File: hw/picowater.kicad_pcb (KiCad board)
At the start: 2 copper layers, 80 x 58.8 mm, 7 parts, among them J1 Conn_01x04_MountingPin, J2 Conn_01x02_MountingPin, J3 Conn_01x06_Pin, U1 Pico

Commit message: v0.1
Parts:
- added J4: UART, Connector_PinHeader_2.54mm:PinHeader_1x03_P2.54mm_Vertical, F.Cu at (105.5, 114.2)
- moved J3 51.3 mm to (70.5, 118.5), turned to -90 degrees
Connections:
- J3 pad 1: GND -> unconnected-(J3-Pin_1-Pad1)
- J3 pad 2: unconnected-(J3-Pin_2-Pad2) -> Net-(J3-Pin_2)
- J3 pad 5: Net-(J3-Pin_5) -> unconnected-(J3-Pin_5-Pad5)
- J3 pad 6: unconnected-(J3-Pin_6-Pad6) -> GND
- U1 pad 14: Net-(J3-Pin_5) -> Net-(J3-Pin_4)
- U1 pad 15: Net-(J3-Pin_4) -> Net-(J3-Pin_3)
- U1 pad 16: Net-(J3-Pin_3) -> Net-(J3-Pin_2)
- U1 pad 21: unconnected-(U1-GPIO16-Pad21) -> Net-(J4-Pin_3)
- U1 pad 22: unconnected-(U1-GPIO17-Pad22) -> Net-(J4-Pin_2)
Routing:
- net Net-(J3-Pin_5): track 41.3 -> 0.00 mm
- net Net-(J3-Pin_3): track 51.4 -> 19.5 mm
- net Net-(J3-Pin_4): track 44.9 -> 23.1 mm
- net Net-(J3-Pin_2): track 0.00 -> 15.9 mm
- net +5V: track 59.0 -> 43.5 mm
- net Net-(J4-Pin_3): track 0.00 -> 7.72 mm
- net Net-(J4-Pin_2): track 0.00 -> 7.72 mm
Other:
- board text added: "+"
- board text added: "5v"
- board text added: "GND"
- board text added: "RX"
- board text added: "TX"
- board text added: "v0.1"

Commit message: update PCB+code
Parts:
- added D1: 1A 20V Schottky, Diode_SMD:D_SOD-123F, B.Cu at (106.0, 73.5)
- added D2: green, LED_THT:LED_D3.0mm, F.Cu at (71.0, 67.8)
- added H1: MountingHole, MountingHole:MountingHole_2.5mm, F.Cu at (55.0, 67.8)
- added H2: MountingHole, MountingHole:MountingHole_2.5mm, F.Cu at (119.0, 68.0)
- added H3: MountingHole, MountingHole:MountingHole_2.5mm, F.Cu at (54.8, 119.8)
- added H4: MountingHole, MountingHole:MountingHole_2.5mm, F.Cu at (128.0, 119.2)
- added J5: Power Out, Connector_PinHeader_2.54mm:PinHeader_1x02_P2.54mm_Vertical, F.Cu at (129.2, 109.5)
- added R3: 330, Resistor_SMD:R_1206_3216Metric_Pad1.30x1.75mm_HandSolder, B.Cu at (66.2, 67.8)
- J2: value Conn_01x02_MountingPin -> Power In
- J3: value Conn_01x06_Pin -> RTC
- moved J3 3.26 mm to (70.2, 115.2)
- moved J2 2.27 mm to (119.7, 119.8)
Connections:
- net Net-(J4-Pin_2) renamed /RX
- net Net-(J4-Pin_3) renamed /TX
- J3 pad 2: Net-(J3-Pin_2) -> /SQW
- J3 pad 3: Net-(J3-Pin_3) -> /SCL
- J3 pad 4: Net-(J3-Pin_4) -> /SDA
- J3 pad 5: unconnected-(J3-Pin_5-Pad5) -> +3.3V
- U1 pad 1: unconnected-(U1-GPIO0-Pad1) -> Net-(D2-A)
- U1 pad 14: Net-(J3-Pin_4) -> unconnected-(U1-GPIO10-Pad14)
- U1 pad 15: Net-(J3-Pin_3) -> /SQW
- U1 pad 16: Net-(J3-Pin_2) -> /SDA
- U1 pad 17: unconnected-(U1-GPIO13-Pad17) -> /SCL
- U1 pad 33: unconnected-(U1-AGND-Pad33) -> GND
- U1 pad 36: unconnected-(U1-3V3-Pad36) -> +3.3V
- U1 pad 39: +5V -> Net-(D1-K)
- U1 pad 42: unconnected-(U1-GND-Pad42) -> GND
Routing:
- net +3.3V: track 0.00 -> 52.5 mm
- net Net-(J3-Pin_4): track 23.1 -> 0.00 mm
- net /SQW: track 0.00 -> 21.2 mm
- net /SDA: track 0.00 -> 19.9 mm
- net Net-(J3-Pin_3): track 19.5 -> 0.00 mm
- net /SCL: track 0.00 -> 16.3 mm
- net Net-(J3-Pin_2): track 15.9 -> 0.00 mm
- net Net-(D2-A): track 0.00 -> 7.85 mm
- net Net-(D1-K): track 0.00 -> 6.84 mm
- net +5V: track 43.5 -> 36.9 mm
- net +12V: track 29.6 -> 34.3 mm
- net Net-(D2-K): track 0.00 -> 3.16 mm
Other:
- board text added: "+12V"
- board text added: "+12VIN"
- board text added: "v0.2"
- board text removed: "v0.1"

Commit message: pcb update
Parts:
- removed J3: RTC, Connector_PinSocket_2.54mm:PinSocket_1x06_P2.54mm_Horizontal
- added J6: RTC, Connector_PinSocket_2.54mm:PinSocket_1x06_P2.54mm_Horizontal, F.Cu at (70.2, 115.2)
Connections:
- U1 pad 14: unconnected-(U1-GPIO10-Pad14) -> Net-(J6-Pin_2)
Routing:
- net +3.3V: track 52.5 -> 0.00 mm
- net Net-(J6-Pin_2): track 0.00 -> 24.6 mm

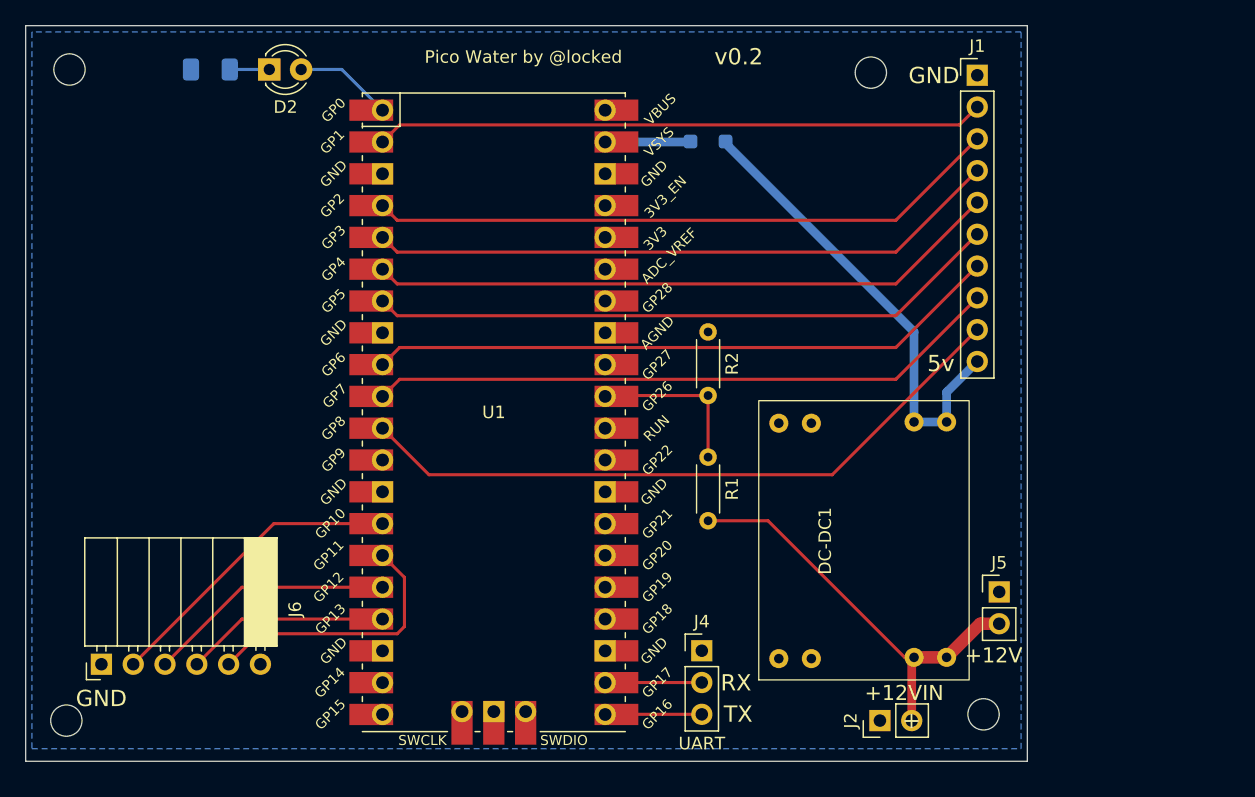
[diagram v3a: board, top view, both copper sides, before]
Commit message: use external RTC for wakeup
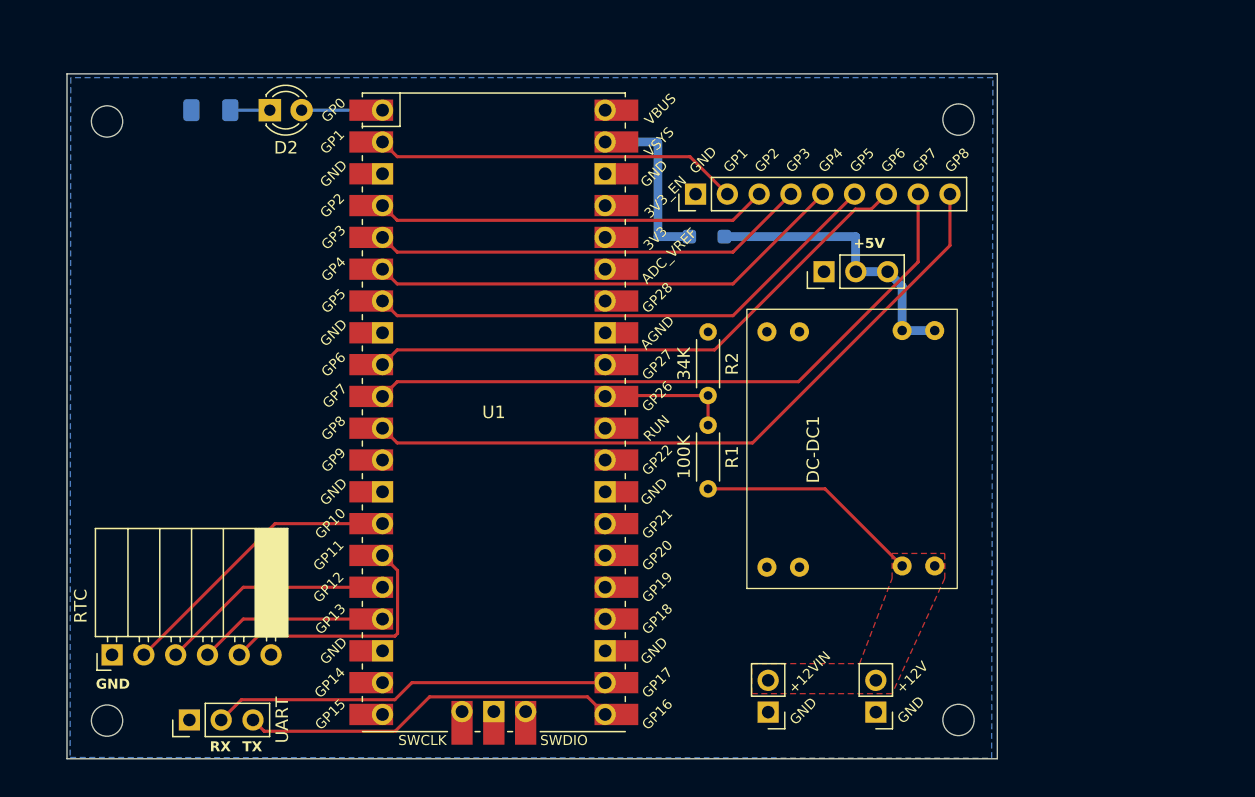
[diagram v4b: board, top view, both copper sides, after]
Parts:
- added J3: +5V Pins, Connector_PinHeader_2.54mm:PinHeader_1x03_P2.54mm_Vertical, F.Cu at (115.3, 83.9)
- added REF**: OSHW-Logo2_9.8x8mm_SilkScreen, Symbol:OSHW-Logo2_9.8x8mm_SilkScreen, B.Cu at (65.8, 94.9)
- J1: value Conn_01x04_MountingPin -> GPIO Pins; footprint Connector_PinHeader_2.54mm:PinHeader_1x10_P2.54mm_Vertical -> Connector_PinHeader_2.54mm:PinHeader_1x09_P2.54mm_Vertical
- moved J4 41.3 mm to (64.6, 119.7), turned to 90 degrees
- moved J1 24.4 mm to (105.0, 77.7), turned to 90 degrees
- moved J5 13.8 mm to (119.4, 119.1), turned to 180 degrees
- moved J2 8.95 mm to (110.8, 119.1), turned to 180 degrees
- moved H2 7.94 mm to (126.0, 71.8)
- moved D1 7.60 mm to (105.9, 81.1)
- moved DC-DC1 7.36 mm to (117.4, 98.1)
- moved H1 5.12 mm to (58.0, 71.9)
- moved D2 3.25 mm to (71.0, 71.0)
- moved R3 3.25 mm to (66.3, 71.0)
- moved H3 3.25 mm to (58.0, 119.8)
- moved R1 2.55 mm to (106.0, 96.2)
- moved H4 2.05 mm to (126.0, 119.7)
- moved J6 1.13 mm to (71.1, 114.5)
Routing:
- net /RX: track 7.72 -> 31.9 mm
- net /TX: track 7.72 -> 30.2 mm
- net GPIO1: track 48.7 -> 29.3 mm
- net GPIO2: track 50.7 -> 31.4 mm
- net +12V: track 34.3 -> 18.1 mm
- net GPIO3: track 50.7 -> 35.0 mm
- net +5V: track 36.9 -> 23.6 mm
- net GPIO4: track 50.7 -> 38.6 mm
- net GPIO5: track 50.7 -> 42.2 mm
- net Net-(D1-K): track 6.84 -> 14.2 mm
- net GPIO6: track 50.8 -> 45.9 mm
- net ADC0: track 13.3 -> 10.6 mm
- net GPIO8: track 53.8 -> 56.4 mm
- net GPIO7: track 50.8 -> 52.6 mm
- net /SQW: track 21.7 -> 20.1 mm
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- added copper zone on F.Cu, net +12V
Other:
- board size 80 x 58.8 mm -> 74.3 x 54.7 mm
- board text added: "+5V"
- board text added: "GP1"
- board text added: "GP2"
- board text added: "GP3"
- board text added: "GP4"
- board text added: "GP5"
- board text added: "GP6"
- board text added: "GP7"
- board text added: "GP8"
- board text added: "https://github.com/locked/picowater"
- board text added: "v0.3"
- board text removed: "+"
- board text removed: "5v"
- board text removed: "v0.2"

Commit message: update pcb
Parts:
- removed REF**: OSHW-Logo2_9.8x8mm_SilkScreen, Symbol:OSHW-Logo2_9.8x8mm_SilkScreen
- added J7: GPIO2, Connector_PinHeader_2.54mm:PinHeader_1x06_P2.54mm_Vertical, F.Cu at (105.4, 119.1)
- added JP1: VCC solder jump, Jumper:SolderJumper-2_P1.3mm_Open_Pad1.0x1.5mm, B.Cu at (71.0, 104.0)
- J1: value GPIO Pins -> GPIO1
- moved J2 1.35 mm to (112.2, 119.1)
- renumbered DC-DC1 to DC-DC
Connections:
- U1 pad 14: Net-(J6-Pin_2) -> /VCC
- U1 pad 15: /SQW -> unconnected-(U1-GPIO11-Pad15)
- U1 pad 19: unconnected-(U1-GPIO14-Pad19) -> /SQW
- U1 pad 24: unconnected-(U1-GPIO18-Pad24) -> Net-(J7-Pin_2)
- U1 pad 25: unconnected-(U1-GPIO19-Pad25) -> Net-(J7-Pin_3)
- U1 pad 26: unconnected-(U1-GPIO20-Pad26) -> Net-(J7-Pin_4)
- U1 pad 27: unconnected-(U1-GPIO21-Pad27) -> Net-(J7-Pin_5)
- U1 pad 29: unconnected-(U1-GPIO22-Pad29) -> Net-(J7-Pin_6)
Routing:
- net Net-(J7-Pin_6): track 0.00 -> 11.5 mm
- net Net-(J7-Pin_5): track 0.00 -> 9.65 mm
- net Net-(J7-Pin_4): track 0.00 -> 9.65 mm
- net Net-(J7-Pin_3): track 0.00 -> 9.65 mm
- net Net-(J7-Pin_2): track 0.00 -> 9.65 mm
- net Net-(J6-Pin_2): track 23.4 -> 14.4 mm
- net /VCC: track 0.00 -> 8.31 mm
- net /SQW: track 20.1 -> 12.4 mm
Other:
- board text added: "GP18"
- board text added: "GP19"
- board text added: "GP20"
- board text added: "GP21"
- board text added: "GP22"
- board text added: "SCL"
- board text added: "SDA"
- board text added: "SQW"
- board text added: "VCC"

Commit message: [hw] update pcb
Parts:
- removed DC-DC: ~, Lunasys_Library:MP1584EN DC-DC 3A Step-Down
- added DC-DC1: ~, Lunasys_Library:MP1584EN DC-DC 3A Step-Down, F.Cu at (113.5, 98.2)
- added J8: +3.3V Pins, Connector_PinHeader_2.54mm:PinHeader_1x03_P2.54mm_Vertical, F.Cu at (117.6, 71.7)
- J1: value GPIO1 -> GPIO Pins
- R1, R2: footprint Resistor_THT:R_Axial_DIN0204_L3.6mm_D1.6mm_P5.08mm_Horizontal -> Resistor_THT:R_Axial_DIN0204_L3.6mm_D1.6mm_P7.62mm_Horizontal
- moved J5 25.9 mm to (125.9, 94.0)
- moved J2 17.9 mm to (125.9, 107.6)
- moved R1 8.31 mm to (113.5, 99.8)
- moved R2 4.32 mm to (108.3, 92.3)
- moved J7 2.16 mm to (107.5, 118.4), turned to 90 degrees
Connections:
- J1 pad 8: GPIO7 -> ADC2
- J1 pad 9: GPIO8 -> ADC1
- J7 pad 6: Net-(J7-Pin_6) -> +5V
- U1 pad 10: GPIO7 -> unconnected-(U1-GPIO7-Pad10)
- U1 pad 11: GPIO8 -> unconnected-(U1-GPIO8-Pad11)
- U1 pad 29: Net-(J7-Pin_6) -> unconnected-(U1-GPIO22-Pad29)
- U1 pad 32: unconnected-(U1-GPIO27_ADC1-Pad32) -> ADC1
- U1 pad 34: unconnected-(U1-GPIO28_ADC2-Pad34) -> ADC2
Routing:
- net GPIO8: track 56.4 -> 0.00 mm
- net GPIO7: track 52.6 -> 0.00 mm
- net ADC1: track 0.00 -> 34.9 mm
- net ADC2: track 0.00 -> 30.1 mm
- net +3.3V: track 0.00 -> 27.7 mm
- net +5V: track 23.6 -> 45.5 mm
- net Net-(J7-Pin_5): track 9.65 -> 25.8 mm
- net Net-(J7-Pin_4): track 9.65 -> 22.2 mm
- net Net-(J7-Pin_6): track 11.5 -> 0.00 mm
- net +12V: track 18.1 -> 29.1 mm
- net Net-(J7-Pin_3): track 9.65 -> 18.6 mm
- net ADC0: track 10.6 -> 18.2 mm
- net Net-(J7-Pin_2): track 9.65 -> 15.0 mm
- net /TX: track 30.2 -> 29.0 mm
- added copper zone on B.Cu, net +5V
- removed copper zone on F.Cu, net +12V
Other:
- board size 74.3 x 54.7 mm -> 74.3 x 55.5 mm
- board text added: "+3.3V"
- board text added: "ADC1"
- board text added: "ADC2"
- board text removed: "GP18"
- board text removed: "GP19"
- board text removed: "GP20"
- board text removed: "GP21"
- board text removed: "GP22"
- board text removed: "GP7"
- board text removed: "GP8"

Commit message: [hw] v0.3 release
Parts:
- removed J8: +3.3V Pins, Connector_PinHeader_2.54mm:PinHeader_1x03_P2.54mm_Vertical
- J1: footprint Connector_PinHeader_2.54mm:PinHeader_1x09_P2.54mm_Vertical -> Connector_PinHeader_2.54mm:PinHeader_2x09_P2.54mm_Vertical
- moved J1 0.61 mm to (104.9, 78.3)
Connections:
- J1 pad 1: GND -> +3.3V
- J1 pad 2: GPIO1 -> GND
- J1 pad 3: GPIO2 -> GPIO1
- J1 pad 4: GPIO3 -> GND
- J1 pad 5: GPIO4 -> GPIO2
- J1 pad 6: GPIO5 -> GND
- J1 pad 7: GPIO6 -> GPIO3
- J1 pad 8: ADC2 -> GND
- J1 pad 9: ADC1 -> GPIO4
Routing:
- net +3.3V: track 27.7 -> 21.4 mm
- net GPIO6: track 46.3 -> 48.4 mm
- net ADC1: track 34.9 -> 36.9 mm
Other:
- board text added: "GNDs"
